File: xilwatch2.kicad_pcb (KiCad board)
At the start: 2 copper layers, 45 x 50 mm, 55 parts, among them J1 Conn_SWD, J2 USB_B_Micro, M1 Vibrator, Q1 NTR5103N, SW1 Btn_Up, SW2 Btn_Down, SW3 Btn_Select, SW4 Btn_Back, U1 ATSAMD21J18A-MU, U2 MCP1700-3302E, U3 LIS3DH, U4 LPH7366, U5 26VF0168IS2AE, U6 RFM69HCW, U7 PAM8301

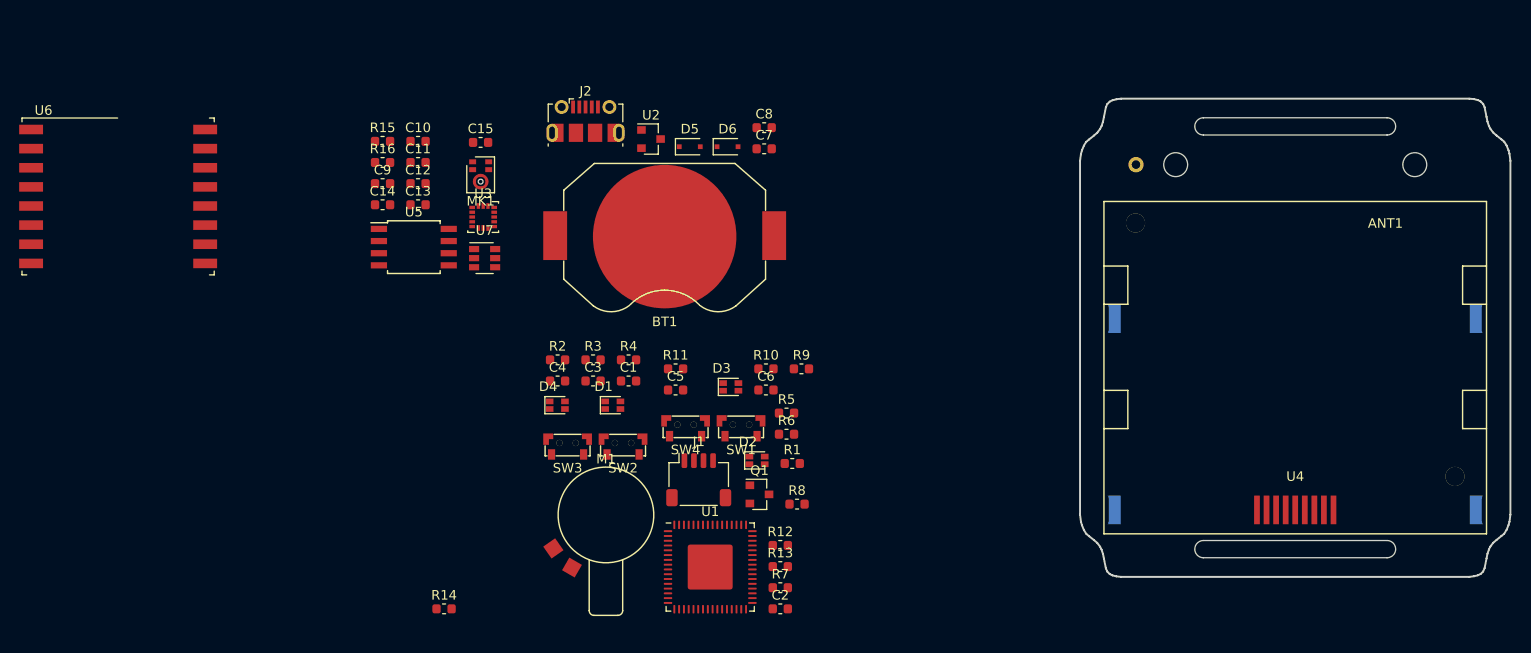
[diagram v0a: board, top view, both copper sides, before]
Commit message: Change of plans, now a nRF52840 with E-ink
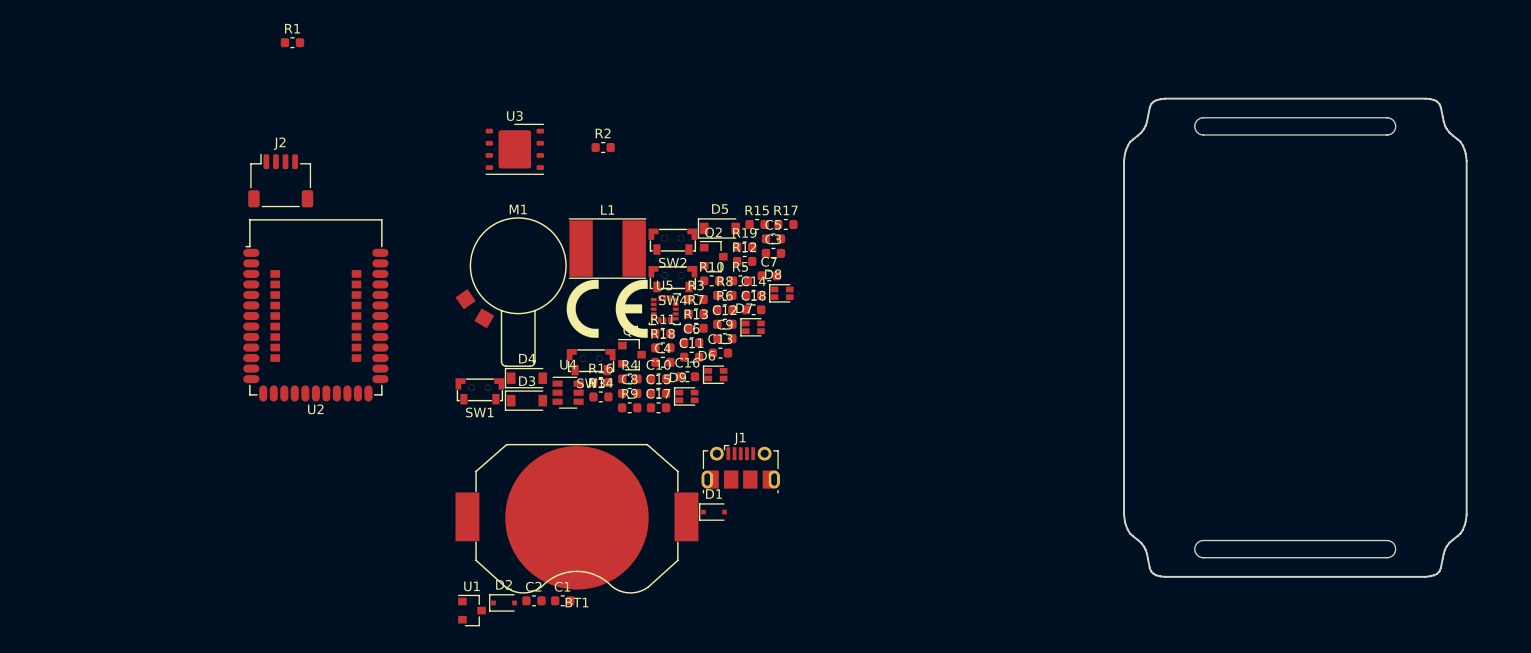
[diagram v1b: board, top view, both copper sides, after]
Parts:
- removed ANT1: ACAG1204-433-T, RF_Antenna_Extra:W3127
- removed MK1: SPH0641LM4H, Sensor_Audio_Extra:SPH0641LM4H
- removed U6: RFM69HCW, RF_Module:HOPERF_RFM69HW
- removed U7: PAM8301, Package_TO_SOT_SMD:SOT-23-6
- added C16: 1uF, Capacitor_SMD:C_0603_1608Metric, F.Cu at (158.6, 88.1)
- added C17: 1uF, Capacitor_SMD:C_0603_1608Metric, F.Cu at (155.5, 91.3)
- added C18: 0.1uF, Capacitor_SMD:C_0603_1608Metric, F.Cu at (165.5, 81.1)
- added D7: LED_TopRight, LED_SMD_Extra:LED_RGBA_0606, F.Cu at (165.4, 82.9)
- added D8: LED_BottomLeft, LED_SMD_Extra:LED_RGBA_0606, F.Cu at (168.5, 79.4)
- added D9: LED_BottomRight, LED_SMD_Extra:LED_RGBA_0606, F.Cu at (158.5, 90.1)
- added L1: 10uH 1A, Inductor_SMD:L_Taiyo-Yuden_NR-60xx_HandSoldering, F.Cu at (150.2, 74.7)
- added LS1: Speaker, Symbol:CE-Logo_8.5x6mm_SilkScreen, F.Cu at (150.2, 81.0)
- added Q2: NTR5103N, Package_TO_SOT_SMD:SOT-23, F.Cu at (161.3, 75.5)
- added R17: 360R, Resistor_SMD:R_0603_1608Metric, F.Cu at (168.8, 72.2)
- added R18: 360R, Resistor_SMD:R_0603_1608Metric, F.Cu at (156.0, 85.1)
- added R19: 360R, Resistor_SMD:R_0603_1608Metric, F.Cu at (164.5, 74.5)
- C1, C10, C11, C12, C13, C14, C15, C9: value 0.1uF -> 1uF
- C2: value 4.7uF -> 1uF
- C3: value 0.1uF -> 4.7uF
- C6: value 1uF -> 0.1uF
- C7: value 1uF -> 4.7uF
- D1: value LED_TopLeft -> S1JHE; footprint LED_SMD_Extra:LED_RGBA_0606 -> Diode_SMD:D_SOD-323F
- D2: value LED_TopRight -> S1JHE; footprint LED_SMD_Extra:LED_RGBA_0606 -> Diode_SMD:D_SOD-323F
- D3: value LED_BottomLeft -> MBR0530; footprint LED_SMD_Extra:LED_RGBA_0606 -> Diode_SMD:D_SOD-123
- D4: value LED_BottomRight -> MBR0530; footprint LED_SMD_Extra:LED_RGBA_0606 -> Diode_SMD:D_SOD-123
- D5: value S1JHE -> MBR0530; footprint Diode_SMD:D_SOD-323F -> Diode_SMD:D_SOD-123
- D6: value S1JHE -> LED_TopLeft; footprint Diode_SMD:D_SOD-323F -> LED_SMD_Extra:LED_RGBA_0606
- J1: value Conn_SWD -> USB_B_Micro; footprint Connector_JST:JST_SH_SM04B-SRSS-TB_1x04-1MP_P1.00mm_Horizontal -> Connector_USB:USB_Micro-B_Molex-105017-0001
- J2: value USB_B_Micro -> Conn_SWD; footprint Connector_USB:USB_Micro-B_Molex-105017-0001 -> Connector_JST:JST_SH_SM04B-SRSS-TB_1x04-1MP_P1.00mm_Horizontal
- Q1: value NTR5103N -> Si1308
- R1: value 1K -> 360R
- R14, R15: value 10K -> 360R
- R16: value 17K -> 360R
- R3, R6, R7: value 360R -> 10K
- R4: value 360R -> 0.47R
- R5: value 360R -> 17K
- U1: value ATSAMD21J18A-MU -> MCP1700-3302E; footprint Package_DFN_QFN:QFN-64-1EP_9x9mm_P0.5mm_EP4.7x4.7mm -> Package_TO_SOT_SMD:SOT-23
- U2: value MCP1700-3302E -> Holyiot_18010; footprint Package_TO_SOT_SMD:SOT-23 -> RF_Module_Extra:Holyiot_18010
- U3: value LIS3DH -> 26VF0168IS2AE; footprint Package_LGA:LGA-16_3x3mm_P0.5mm_LayoutBorder3x5y -> Package_SON:WSON-8-1EP_6x5mm_P1.27mm_EP3.4x4mm
- U4: value LPH7366 -> PAM8301; footprint Display_Extra:Nokia_5110-3310_LCD -> Package_TO_SOT_SMD:SOT-23-6
- U5: value 26VF0168IS2AE -> LIS3DH; footprint Package_SO:SOIJ-8_5.3x5.3mm_P1.27mm -> Package_LGA:LGA-16_3x3mm_P0.5mm_LayoutBorder3x5y
- moved U4 76.1 mm to (146.1, 89.7), turned to 0 degrees
- moved R1 68.3 mm to (117.3, 53.1)
- moved R15 40.1 mm to (165.8, 72.2)
- moved C14 39.9 mm to (165.5, 79.6)
- moved C9 39.3 mm to (162.5, 84.1)
- moved U2 39.2 mm to (119.7, 80.8)
- moved C10 35.4 mm to (155.5, 88.3)
- moved C12 35.3 mm to (162.5, 82.6)
- moved C13 35.2 mm to (162.0, 85.6)
- moved C11 35.1 mm to (159.0, 86.0)
- moved J2 32.5 mm to (116.0, 67.6)
- moved R16 32.4 mm to (149.5, 88.7)
- moved C15 32.2 mm to (155.5, 89.8)
- moved C8 31.1 mm to (152.5, 89.8)
- moved BT1 30.8 mm to (147.0, 102.7)
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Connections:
- C1 pad 1: Net-(C1-Pad1) -> GND
- C1 pad 2: VDD -> Net-(C1-Pad2)
- C10 pad 2: VDD -> Net-(C10-Pad2)
- C12 pad 2: VDD -> Net-(C12-Pad2)
- C13 pad 2: VDD -> Net-(C13-Pad2)
- C14 pad 1: /SPEAKER -> GND
- C15 pad 2: VDD -> Net-(C15-Pad2)
- C2 pad 1: GND -> VDD
- C2 pad 2: VDD -> GND
- C5 pad 1: GND -> /SPEAKER
- C5 pad 2: VDD -> Net-(C5-Pad2)
- C6 pad 2: +1V2 -> VDD
- C7 pad 1: GND -> Net-(C7-Pad1)
- C8 pad 1: VDD -> GND
- C8 pad 2: GND -> VDD
- C9 pad 2: VDD -> Net-(C9-Pad2)
- D1 pad 1: Net-(D1-Pad1) -> VDD
- D1 pad 2: Net-(D1-Pad2) -> +BATT
- D2 pad 1: Net-(D2-Pad1) -> Net-(C1-Pad2)
- D2 pad 2: Net-(D2-Pad2) -> VBUS
- D3 pad 1: Net-(D3-Pad1) -> /Peripherals/PREVGH
- D3 pad 2: Net-(D3-Pad2) -> Net-(C7-Pad1)
- D4 pad 1: Net-(D4-Pad1) -> Net-(C7-Pad2)
- D4 pad 2: Net-(D4-Pad2) -> /Peripherals/PREVGL
- D5 pad 1: VDD -> GND
- D5 pad 2: +BATT -> Net-(C7-Pad2)
- D6 pad 1: Net-(C7-Pad2) -> Net-(D6-Pad1)
- D6 pad 2: VBUS -> Net-(D6-Pad2)
- J1 pad 1: VDD -> VBUS
- J1 pad 2: /SWDCLK -> /USB_D-
- J1 pad 3: GND -> /USB_D+
- J1 pad 4: /SWDIO -> Net-(J1-Pad4)
- J2 pad 1: VBUS -> VDD
- J2 pad 2: /USB_D- -> /SWDCLK
- J2 pad 3: /USB_D+ -> GND
- J2 pad 4: Net-(J2-Pad4) -> /SWDIO
- M1 pad 2: Net-(C1-Pad1) -> Net-(C18-Pad1)
- Q1 pad 1: /VIBRATOR -> /Peripherals/GDR
- Q1 pad 2: GND -> /Peripherals/RESE
- Q1 pad 3: Net-(C1-Pad1) -> Net-(C7-Pad1)
- R1 pad 1: /SWDCLK -> /USB_D+
- R1 pad 2: VDD -> Net-(R1-Pad2)
- R10 pad 1: /LED3_B -> /LED1_B
- R10 pad 2: Net-(D3-Pad3) -> Net-(D6-Pad3)
- R11 pad 1: /LED4_R -> /LED2_R
- R11 pad 2: Net-(D4-Pad1) -> Net-(D7-Pad1)
- R12 pad 1: /LED4_G -> /LED2_G
- R12 pad 2: Net-(D4-Pad2) -> Net-(D7-Pad2)
- R13 pad 1: /LED4_B -> /LED2_B
- R13 pad 2: Net-(D4-Pad3) -> Net-(D7-Pad3)
- R14 pad 1: VDD -> /LED3_R
- R14 pad 2: /ACCEL_SCL -> Net-(D8-Pad1)
- R15 pad 1: VDD -> /LED3_G
- R15 pad 2: /ACCEL_SDA -> Net-(D8-Pad2)
- R16 pad 1: Net-(R16-Pad1) -> /LED3_B
- R16 pad 2: Net-(C14-Pad2) -> Net-(D8-Pad3)
- R2 pad 1: /LED1_R -> /USB_D-
- R2 pad 2: Net-(D1-Pad1) -> Net-(R2-Pad2)
- R3 pad 1: /LED1_G -> GND
- R3 pad 2: Net-(D1-Pad2) -> /Peripherals/GDR
- R4 pad 1: /LED1_B -> GND
- R4 pad 2: Net-(D1-Pad3) -> /Peripherals/RESE
- R5 pad 1: /LED2_R -> Net-(R5-Pad1)
- R5 pad 2: Net-(D2-Pad1) -> Net-(C5-Pad2)
- R6 pad 1: /LED2_G -> VDD
- R6 pad 2: Net-(D2-Pad2) -> /ACCEL_SCL
- R7 pad 1: /LED2_B -> VDD
- R7 pad 2: Net-(D2-Pad3) -> /ACCEL_SDA
- R8 pad 1: /LED3_R -> /LED1_R
- R8 pad 2: Net-(D3-Pad1) -> Net-(D6-Pad1)
- R9 pad 1: /LED3_G -> /LED1_G
- R9 pad 2: Net-(D3-Pad2) -> Net-(D6-Pad2)
- U1 pad 1: /ACCEL_SDA -> GND
- U1 pad 2: /ACCEL_SCL -> VDD
- U1 pad 3: /SPEAKER -> Net-(C1-Pad2)
- U2 pad 2: VDD -> Net-(U2-Pad2)
- U2 pad 3: Net-(C7-Pad2) -> Net-(U2-Pad3)
- U3 pad 1: VDD -> /QSPI_IO3
- U3 pad 2: (no net) -> /QSPI_IO0
- U3 pad 3: (no net) -> /QSPI_CS
- U3 pad 4: /ACCEL_SCL -> GND
- U3 pad 5: GND -> /QSPI_IO1
- U3 pad 6: /ACCEL_SDA -> /QSPI_IO2
- U3 pad 7: VDD -> /QSPI_CLK
- U3 pad 9: Net-(U3-Pad9) -> (no net)
- U4 pad 1: /LCD_RESET -> Net-(LS1-Pad2)
- U4 pad 2: Net-(C11-Pad2) -> GND
- U4 pad 3: GND -> Net-(R5-Pad1)
- U4 pad 4: VDD -> /SPEAKER_SD
- U4 pad 5: /LCD_CS -> VDD
- U4 pad 6: /LCD_DC -> Net-(LS1-Pad1)
- U5 pad 1: /FLASH_CS -> VDD
- U5 pad 2: /FLASH_SO -> (no net)
- U5 pad 3: VDD -> (no net)
- U5 pad 4: GND -> /ACCEL_SCL
- U5 pad 5: /FLASH_SI -> GND
- U5 pad 6: /FLASH_SCK -> /ACCEL_SDA
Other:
- board size 45 x 50 mm -> 35.8 x 50 mm

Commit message: Finish rev1
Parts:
- removed J2: Conn_SWD, Connector_JST:JST_SH_SM04B-SRSS-TB_1x04-1MP_P1.00mm_Horizontal
- added TP1: TP_GND, TestPoint:TestPoint_Pad_D1.0mm, F.Cu at (156.2, 73.7)
- added TP2: TP_VDD, TestPoint:TestPoint_Pad_D1.0mm, F.Cu at (156.8, 71.8)
- added TP3: TP_SWDCLK, TestPoint:TestPoint_Pad_D1.0mm, F.Cu at (153.8, 79.5)
- added TP4: TP_SWDIO, TestPoint:TestPoint_Pad_D1.0mm, F.Cu at (155.2, 78.0)
- added U6: GDEW0154T8, Connector_GoodDisplay:GoodDisplay_24P-0.5SH_1x24-Horizontal, B.Cu at (164.2, 96.0)
- added X1: SAO, Connector_Badgelife:SAO-2x2, F.Cu at (177.2, 67.2)
- BT1, C1, C10, C11, C12, C13, C14, C15, C16, C17, C18, C2, C3, C7, C8, C9, D1, D2, D3, D4, D5, J1, M1, Q1, Q2, R3, R4, SW1, SW2, SW3, SW4, U1: moved to B.Cu
- L1: footprint Inductor_SMD:L_Taiyo-Yuden_NR-60xx_HandSoldering -> Inductor_SMD:L_Taiyo-Yuden_MD-3030; moved to B.Cu
- LS1: value Speaker -> CMT-5023S-SMT; footprint Symbol:CE-Logo_8.5x6mm_SilkScreen -> Buzzer_Beeper_Extra:CMT-5023S
- R1, R2: value 360R -> 22R
- U3: value 26VF0168IS2AE -> IS25LP128F
- moved R1 57.6 mm to (166.4, 83.1), turned to 180 degrees
- moved SW1 47.2 mm to (181.3, 73.7), turned to 90 degrees
- moved C2 44.9 mm to (150.2, 67.3), turned to 180 degrees
- moved U3 44.3 mm to (164.0, 101.8), turned to 180 degrees
- moved U1 43.8 mm to (153.8, 72.5)
- moved C1 42.9 mm to (150.2, 68.9)
- moved D4 39.4 mm to (180.2, 97.0), turned to 180 degrees
- moved D3 38.5 mm to (180.2, 92.9), turned to 180 degrees
- moved SW2 38.4 mm to (181.2, 103.8), turned to 90 degrees
- moved D2 37.8 mm to (152.0, 76.1), turned to 270 degrees
- moved U2 35.6 mm to (154.4, 88.8), turned to 90 degrees
- moved D1 33.4 mm to (153.8, 69.7)
- moved SW3 32.9 mm to (181.3, 88.8), turned to 90 degrees
- moved D5 32.4 mm to (180.2, 99.4)
- moved L1 32.4 mm to (175.8, 94.6), turned to 270 degrees
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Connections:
- R6 pad 2: /ACCEL_SCL -> /I2C_SCL
- R7 pad 2: /ACCEL_SDA -> /I2C_SDA
- U2 pad 10: Net-(U2-Pad10) -> /QSPI_IO2
- U2 pad 11: Net-(U2-Pad11) -> /QSPI_IO1
- U2 pad 12: Net-(U2-Pad12) -> /QSPI_CS
- U2 pad 13: Net-(U2-Pad13) -> /BTN_DOWN
- U2 pad 17: Net-(U2-Pad17) -> /EINK_SCK
- U2 pad 18: Net-(U2-Pad18) -> /EINK_MOSI
- U2 pad 19: Net-(U2-Pad19) -> /EINK_CS
- U2 pad 2: Net-(U2-Pad2) -> /BTN_BACK
- U2 pad 20: Net-(U2-Pad20) -> /EINK_DC
- U2 pad 21: Net-(U2-Pad21) -> /EINK_RESET
- U2 pad 22: Net-(U2-Pad22) -> /EINK_BUSY
- U2 pad 3: Net-(U2-Pad3) -> /VIBRATOR
- U2 pad 33: Net-(U2-Pad33) -> /LED1_G
- U2 pad 34: Net-(U2-Pad34) -> /LED1_R
- U2 pad 35: Net-(U2-Pad35) -> /LED1_B
- U2 pad 36: Net-(U2-Pad36) -> /SPEAKER_SD
- U2 pad 39: Net-(U2-Pad39) -> /SPEAKER
- U2 pad 4: Net-(U2-Pad4) -> /LED3_G
- U2 pad 40: Net-(U2-Pad40) -> /BTN_UP
- U2 pad 41: Net-(U2-Pad41) -> /LED2_B
- U2 pad 42: Net-(U2-Pad42) -> /LED2_G
- U2 pad 43: Net-(U2-Pad43) -> /LED2_R
- U2 pad 48: Net-(U2-Pad48) -> /BTN_SELECT
- U2 pad 49: Net-(U2-Pad49) -> /ACCEL_INT
- U2 pad 5: Net-(U2-Pad5) -> /LED3_R
- U2 pad 50: Net-(U2-Pad50) -> /I2C_SCL
- U2 pad 51: Net-(U2-Pad51) -> /I2C_SDA
- U2 pad 52: Net-(U2-Pad52) -> /LED4_G
- U2 pad 53: Net-(U2-Pad53) -> /LED4_R
- U2 pad 54: Net-(U2-Pad54) -> /LED4_B
- U2 pad 6: Net-(U2-Pad6) -> /LED3_B
- U2 pad 7: Net-(U2-Pad7) -> /QSPI_IO3
- U2 pad 8: Net-(U2-Pad8) -> /QSPI_CLK
- U2 pad 9: Net-(U2-Pad9) -> /QSPI_IO0
- U3 pad 1: /QSPI_IO3 -> /QSPI_CS
- U3 pad 2: /QSPI_IO0 -> /QSPI_IO1
- U3 pad 3: /QSPI_CS -> /QSPI_IO2
- U3 pad 5: /QSPI_IO1 -> /QSPI_IO0
- U3 pad 6: /QSPI_IO2 -> /QSPI_CLK
- U3 pad 7: /QSPI_CLK -> /QSPI_IO3
- U3 pad 9: (no net) -> GND
- U5 pad 4: /ACCEL_SCL -> /I2C_SCL
- U5 pad 6: /ACCEL_SDA -> /I2C_SDA
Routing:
- net VDD: track 0.00 -> 152.2 mm, vias 0 -> 11
- net /I2C_SDA: track 0.00 -> 51.4 mm, vias 0 -> 2
- net /I2C_SCL: track 0.00 -> 34.7 mm, vias 0 -> 2
- net /BTN_UP: track 0.00 -> 33.1 mm, vias 0 -> 1
- net +BATT: track 0.00 -> 28.0 mm
- net /Peripherals/RESE: track 0.00 -> 27.6 mm
- net /LED2_B: track 0.00 -> 26.5 mm
- net VBUS: track 0.00 -> 26.0 mm, vias 0 -> 1
- net /Peripherals/GDR: track 0.00 -> 25.2 mm
- net /LED2_R: track 0.00 -> 24.8 mm
- net /USB_D-: track 0.00 -> 23.4 mm, vias 0 -> 1
- net /LED2_G: track 0.00 -> 23.3 mm
- net GND: track 0.00 -> 22.5 mm, vias 0 -> 21
- net /USB_D+: track 0.00 -> 22.2 mm, vias 0 -> 1
- net /BTN_DOWN: track 0.00 -> 22.1 mm, vias 0 -> 1
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- added copper zone on B.Cu, net GND
- added copper zone on F.Cu, net GND
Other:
- board size 35.8 x 50 mm -> 37.8 x 50 mm
- net class Default: clearance 0.2 -> 0.16; trace_width 0.25 -> 0.16; via_dia 0.8 -> 0.6; via_drill 0.4 -> 0.35
- net class Power added: clearance 0.2, trace_width 0.25, via_dia 0.6, via_drill 0.35
- rule pad_to_mask_clearance: 0.2 -> 0.16
- rule trace_clearance: 0.2 -> 0.16
- rule trace_min: 0.2 -> 0.16
- board text added: "1.2mm PCB!"
- board text added: "CLK"
- board text added: "GND"
- board text added: "IO"
- board text added: "VDD"
